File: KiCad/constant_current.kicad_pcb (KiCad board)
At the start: 2 copper layers, 15.2 x 16.5 mm, 18 parts, among them Q1 BC817-40

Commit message: Minor Layout changes
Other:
- board text added: "rev06092017"
- board text removed: "rev05092017"
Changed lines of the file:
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@@
   (general
     (links 24)
-    (no_connects 0)
+    (no_connects 1)
     (area 109.144999 56.439999 124.535001 73.100001)
     (thickness 1.6)
@@
     (effects (font (size 0.7 0.7) (thickness 0.1)) (justify mirror))
   )
-  (gr_text "rev05092017\n" (at 113.538 71.755) (layer B.SilkS)
+  (gr_text "rev06092017\n" (at 113.538 71.755) (layer B.SilkS)
     (effects (font (size 0.7 0.7) (thickness 0.1)) (justify mirror))
   )

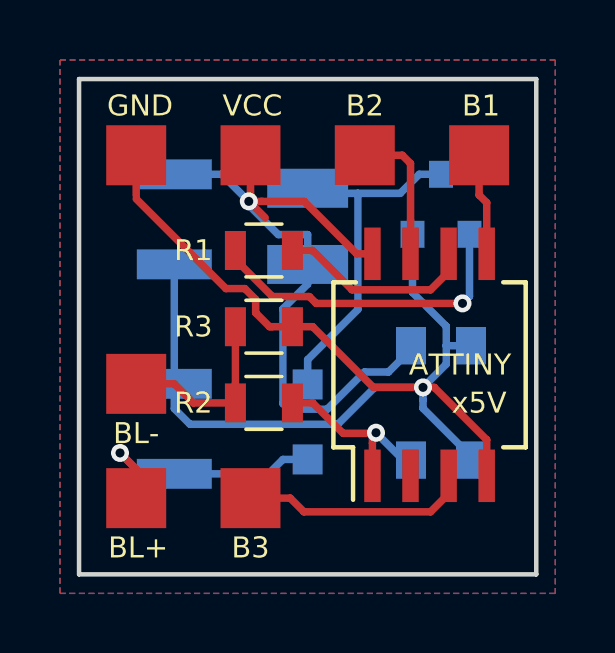
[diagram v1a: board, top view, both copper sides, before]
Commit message: changed diode footprint
Changed the diode footprint to Minimelf
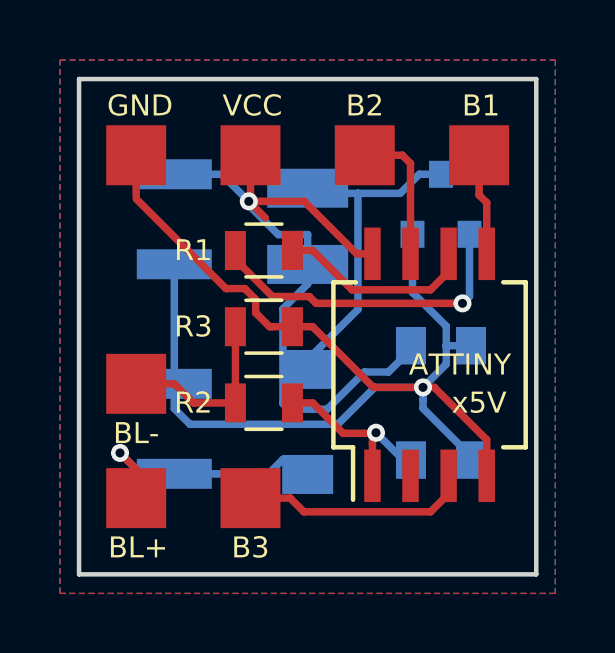
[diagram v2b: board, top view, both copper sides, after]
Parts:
- D1: footprint Diodes_SMD:D_SOD-323_HandSoldering -> Diodes_SMD:D_MiniMELF
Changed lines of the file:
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@@
     (pad_to_mask_clearance 0)
     (aux_axis_origin 0 0)
-    (visible_elements 7FFFFF5F)
+    (visible_elements 7FFFFD5F)
     (pcbplotparams
       (layerselection 0x010fc_80000001)
@@
     )
   )
-  (module Diodes_SMD:D_SOD-323_HandSoldering (layer B.Cu)
-    (at 116.84 67.945 90)
-    (descr SOD-323)
-    (tags SOD-323)
-    (attr smd)
-    (fp_text reference D1 (at 2.54 0 180) (layer B.SilkS)
-      (effects (font (size 0.7 0.7) (thickness 0.1)) (justify mirror))
-    )
-    (fp_text value D (at 0.1 -1.9 90) (layer B.Fab) hide
-      (effects (font (size 1 1) (thickness 0.15)) (justify mirror))
-    )
-    (fp_text user %R (at 0 1.85 90) (layer B.Fab)
-      (effects (font (size 1 1) (thickness 0.15)) (justify mirror))
-    )
-    (fp_line (start -1.9 0.85) (end -1.9 -0.85) (layer B.SilkS) (width 0.12))
-    (fp_line (start 0.2 0) (end 0.45 0) (layer B.Fab) (width 0.1))
-    (fp_line (start 0.2 -0.35) (end -0.3 0) (layer B.Fab) (width 0.1))
-    (fp_line (start 0.2 0.35) (end 0.2 -0.35) (layer B.Fab) (width 0.1))
-    (fp_line (start -0.3 0) (end 0.2 0.35) (layer B.Fab) (width 0.1))
-    (fp_line (start -0.3 0) (end -0.5 0) (layer B.Fab) (width 0.1))
-    (fp_line (start -0.3 0.35) (end -0.3 -0.35) (layer B.Fab) (width 0.1))
-    (fp_line (start -0.9 -0.7) (end -0.9 0.7) (layer B.Fab) (width 0.1))
-    (fp_line (start 0.9 -0.7) (end -0.9 -0.7) (layer B.Fab) (width 0.1))
-    (fp_line (start 0.9 0.7) (end 0.9 -0.7) (layer B.Fab) (width 0.1))
-    (fp_line (start -0.9 0.7) (end 0.9 0.7) (layer B.Fab) (width 0.1))
-    (fp_line (start -2 0.95) (end 2 0.95) (layer B.CrtYd) (width 0.05))
-    (fp_line (start 2 0.95) (end 2 -0.95) (layer B.CrtYd) (width 0.05))
-    (fp_line (start -2 -0.95) (end 2 -0.95) (layer B.CrtYd) (width 0.05))
-    (fp_line (start -2 0.95) (end -2 -0.95) (layer B.CrtYd) (width 0.05))
-    (fp_line (start -1.9 -0.85) (end 1.25 -0.85) (layer B.SilkS) (width 0.12))
-    (fp_line (start -1.9 0.85) (end 1.25 0.85) (layer B.SilkS) (width 0.12))
-    (pad 1 smd rect (at -1.25 0 90) (size 1 1) (layers B.Cu B.Paste B.Mask)
-      (net 11 "Net-(C2-Pad1)"))
-    (pad 2 smd rect (at 1.25 0 90) (size 1 1) (layers B.Cu B.Paste B.Mask)
-      (net 3 "Net-(D1-Pad2)"))
-    (model ${KISYS3DMOD}/Diodes_SMD.3dshapes/D_SOD-323.wrl
-      (at (xyz 0 0 0))
-      (scale (xyz 1 1 1))
-      (rotate (xyz 0 0 0))
-    )
-  )
   (module Capacitors_SMD:C_1210 (layer B.Cu)
     (at 112.395 61.19 90)
@@
     )
   )
-  (gr_line (start 115.951 70.231) (end 117.729 70.231) (layer B.SilkS) (width 0.2))
+  (module Diodes_SMD:D_MiniMELF (layer B.Cu)
+    (at 116.84 67.945 90)
+    (descr "Diode Mini-MELF")
+    (tags "Diode Mini-MELF")
+    (attr smd)
+    (fp_text reference D1 (at 3.1115 0 180) (layer B.SilkS)
+      (effects (font (size 0.7 0.7) (thickness 0.1)) (justify mirror))
+    )
+    (fp_text value D (at 0 -1.75 90) (layer B.Fab)
+      (effects (font (size 1 1) (thickness 0.15)) (justify mirror))
+    )
+    (fp_text user %R (at 0 2 90) (layer B.Fab)
+      (effects (font (size 1 1) (thickness 0.15)) (justify mirror))
+    )
+    (fp_line (start 1.75 1) (end -2.55 1) (layer B.SilkS) (width 0.12))
+    (fp_line (start -2.55 1) (end -2.55 -1) (layer B.SilkS) (width 0.12))
+    (fp_line (start -2.55 -1) (end 1.75 -1) (layer B.SilkS) (width 0.12))
+    (fp_line (start 1.65 0.8) (end 1.65 -0.8) (layer B.Fab) (width 0.1))
+    (fp_line (start 1.65 -0.8) (end -1.65 -0.8) (layer B.Fab) (width 0.1))
+    (fp_line (start -1.65 -0.8) (end -1.65 0.8) (layer B.Fab) (width 0.1))
+    (fp_line (start -1.65 0.8) (end 1.65 0.8) (layer B.Fab) (width 0.1))
+    (fp_line (start 0.25 0) (end 0.75 0) (layer B.Fab) (width 0.1))
+    (fp_line (start 0.25 -0.4) (end -0.35 0) (layer B.Fab) (width 0.1))
+    (fp_line (start 0.25 0.4) (end 0.25 -0.4) (layer B.Fab) (width 0.1))
+    (fp_line (start -0.35 0) (end 0.25 0.4) (layer B.Fab) (width 0.1))
+    (fp_line (start -0.35 0) (end -0.35 -0.55) (layer B.Fab) (width 0.1))
+    (fp_line (start -0.35 0) (end -0.35 0.55) (layer B.Fab) (width 0.1))
+    (fp_line (start -0.75 0) (end -0.35 0) (layer B.Fab) (width 0.1))
+    (fp_line (start -2.65 1.1) (end 2.65 1.1) (layer B.CrtYd) (width 0.05))
+    (fp_line (start 2.65 1.1) (end 2.65 -1.1) (layer B.CrtYd) (width 0.05))
+    (fp_line (start 2.65 -1.1) (end -2.65 -1.1) (layer B.CrtYd) (width 0.05))
+    (fp_line (start -2.65 -1.1) (end -2.65 1.1) (layer B.CrtYd) (width 0.05))
+    (pad 1 smd rect (at -1.75 0 90) (size 1.3 1.7) (layers B.Cu B.Paste B.Mask)
+      (net 11 "Net-(C2-Pad1)"))
+    (pad 2 smd rect (at 1.75 0 90) (size 1.3 1.7) (layers B.Cu B.Paste B.Mask)
+      (net 3 "Net-(D1-Pad2)"))
+    (model ${KISYS3DMOD}/Diodes_SMD.3dshapes/D_MiniMELF.wrl
+      (at (xyz 0 0 0))
+      (scale (xyz 1 1 1))
+      (rotate (xyz 0 0 0))
+    )
+  )
+  (gr_line (start 115.7605 70.8025) (end 117.9195 70.8025) (layer B.SilkS) (width 0.2))
   (gr_text rcb_4s (at 121.92 71.755) (layer B.SilkS)
     (effects (font (size 0.7 0.7) (thickness 0.1)) (justify mirror))

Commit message: Code and Layout fixes
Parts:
- D1: footprint Diodes_SMD:D_MiniMELF -> Diodes_SMD:D_SOD-323_HandSoldering
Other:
- board text added: "rev14092017"
- board text removed: "rev06092017"
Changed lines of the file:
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@@
     (links 24)
     (no_connects 1)
-    (area 109.144999 56.439999 124.535001 73.100001)
+    (area 108.585 54.57988 126.109 73.660001)
     (thickness 1.6)
     (drawings 8)
@@
     (pad_to_mask_clearance 0)
     (aux_axis_origin 0 0)
-    (visible_elements 7FFFFD5F)
+    (visible_elements 7FFFFD7F)
     (pcbplotparams
       (layerselection 0x010fc_80000001)
@@
       (drillshape 0)
       (scaleselection 1)
-      (outputdirectory gerber/panel/))
+      (outputdirectory ../gerber/))
   )
   (net 0 "")
@@
     (tags "capacitor 1210")
     (attr smd)
-    (fp_text reference C1 (at 2.667 0 180) (layer B.SilkS)
+    (fp_text reference C1 (at 2.77 0 180) (layer B.SilkS)
       (effects (font (size 0.7 0.7) (thickness 0.1)) (justify mirror))
     )
@@
     )
   )
-  (module Diodes_SMD:D_MiniMELF (layer B.Cu)
+  (module Diodes_SMD:D_SOD-323_HandSoldering (layer B.Cu)
     (at 116.84 67.945 90)
-    (descr "Diode Mini-MELF")
-    (tags "Diode Mini-MELF")
-    (attr smd)
-    (fp_text reference D1 (at 3.1115 0 180) (layer B.SilkS)
+    (descr SOD-323)
+    (tags SOD-323)
+    (attr smd)
+    (fp_text reference D1 (at 2.54 0 180) (layer B.SilkS)
       (effects (font (size 0.7 0.7) (thickness 0.1)) (justify mirror))
     )
-    (fp_text value D (at 0 -1.75 90) (layer B.Fab)
-      (effects (font (size 1 1) (thickness 0.15)) (justify mirror))
-    )
-    (fp_text user %R (at 0 2 90) (layer B.Fab)
-      (effects (font (size 1 1) (thickness 0.15)) (justify mirror))
-    )
-    (fp_line (start 1.75 1) (end -2.55 1) (layer B.SilkS) (width 0.12))
-    (fp_line (start -2.55 1) (end -2.55 -1) (layer B.SilkS) (width 0.12))
-    (fp_line (start -2.55 -1) (end 1.75 -1) (layer B.SilkS) (width 0.12))
-    (fp_line (start 1.65 0.8) (end 1.65 -0.8) (layer B.Fab) (width 0.1))
-    (fp_line (start 1.65 -0.8) (end -1.65 -0.8) (layer B.Fab) (width 0.1))
-    (fp_line (start -1.65 -0.8) (end -1.65 0.8) (layer B.Fab) (width 0.1))
-    (fp_line (start -1.65 0.8) (end 1.65 0.8) (layer B.Fab) (width 0.1))
-    (fp_line (start 0.25 0) (end 0.75 0) (layer B.Fab) (width 0.1))
-    (fp_line (start 0.25 -0.4) (end -0.35 0) (layer B.Fab) (width 0.1))
-    (fp_line (start 0.25 0.4) (end 0.25 -0.4) (layer B.Fab) (width 0.1))
-    (fp_line (start -0.35 0) (end 0.25 0.4) (layer B.Fab) (width 0.1))
-    (fp_line (start -0.35 0) (end -0.35 -0.55) (layer B.Fab) (width 0.1))
-    (fp_line (start -0.35 0) (end -0.35 0.55) (layer B.Fab) (width 0.1))
-    (fp_line (start -0.75 0) (end -0.35 0) (layer B.Fab) (width 0.1))
-    (fp_line (start -2.65 1.1) (end 2.65 1.1) (layer B.CrtYd) (width 0.05))
-    (fp_line (start 2.65 1.1) (end 2.65 -1.1) (layer B.CrtYd) (width 0.05))
-    (fp_line (start 2.65 -1.1) (end -2.65 -1.1) (layer B.CrtYd) (width 0.05))
-    (fp_line (start -2.65 -1.1) (end -2.65 1.1) (layer B.CrtYd) (width 0.05))
-    (pad 1 smd rect (at -1.75 0 90) (size 1.3 1.7) (layers B.Cu B.Paste B.Mask)
+    (fp_text value D (at 0.1 -1.9 90) (layer B.Fab)
+      (effects (font (size 1 1) (thickness 0.15)) (justify mirror))
+    )
+    (fp_text user %R (at 0 1.85 90) (layer B.Fab)
+      (effects (font (size 1 1) (thickness 0.15)) (justify mirror))
+    )
+    (fp_line (start -1.9 0.85) (end -1.9 -0.85) (layer B.SilkS) (width 0.12))
+    (fp_line (start 0.2 0) (end 0.45 0) (layer B.Fab) (width 0.1))
+    (fp_line (start 0.2 -0.35) (end -0.3 0) (layer B.Fab) (width 0.1))
+    (fp_line (start 0.2 0.35) (end 0.2 -0.35) (layer B.Fab) (width 0.1))
+    (fp_line (start -0.3 0) (end 0.2 0.35) (layer B.Fab) (width 0.1))
+    (fp_line (start -0.3 0) (end -0.5 0) (layer B.Fab) (width 0.1))
+    (fp_line (start -0.3 0.35) (end -0.3 -0.35) (layer B.Fab) (width 0.1))
+    (fp_line (start -0.9 -0.7) (end -0.9 0.7) (layer B.Fab) (width 0.1))
+    (fp_line (start 0.9 -0.7) (end -0.9 -0.7) (layer B.Fab) (width 0.1))
+    (fp_line (start 0.9 0.7) (end 0.9 -0.7) (layer B.Fab) (width 0.1))
+    (fp_line (start -0.9 0.7) (end 0.9 0.7) (layer B.Fab) (width 0.1))
+    (fp_line (start -2 0.95) (end 2 0.95) (layer B.CrtYd) (width 0.05))
+    (fp_line (start 2 0.95) (end 2 -0.95) (layer B.CrtYd) (width 0.05))
+    (fp_line (start -2 -0.95) (end 2 -0.95) (layer B.CrtYd) (width 0.05))
+    (fp_line (start -2 0.95) (end -2 -0.95) (layer B.CrtYd) (width 0.05))
+    (fp_line (start -1.9 -0.85) (end 1.25 -0.85) (layer B.SilkS) (width 0.12))
+    (fp_line (start -1.9 0.85) (end 1.25 0.85) (layer B.SilkS) (width 0.12))
+    (pad 1 smd rect (at -1.25 0 90) (size 1 1) (layers B.Cu B.Paste B.Mask)
       (net 11 "Net-(C2-Pad1)"))
-    (pad 2 smd rect (at 1.75 0 90) (size 1.3 1.7) (layers B.Cu B.Paste B.Mask)
+    (pad 2 smd rect (at 1.25 0 90) (size 1 1) (layers B.Cu B.Paste B.Mask)
       (net 3 "Net-(D1-Pad2)"))
-    (model ${KISYS3DMOD}/Diodes_SMD.3dshapes/D_MiniMELF.wrl
-      (at (xyz 0 0 0))
-      (scale (xyz 1 1 1))
-      (rotate (xyz 0 0 0))
-    )
-  )
-  (gr_line (start 115.7605 70.8025) (end 117.9195 70.8025) (layer B.SilkS) (width 0.2))
+    (model ${KISYS3DMOD}/Diodes_SMD.3dshapes/D_SOD-323.wrl
+      (at (xyz 0 0 0))
+      (scale (xyz 1 1 1))
+      (rotate (xyz 0 0 0))
+    )
+  )
+  (gr_line (start 115.7605 70.2945) (end 117.9195 70.2945) (layer B.SilkS) (width 0.2))
   (gr_text rcb_4s (at 121.92 71.755) (layer B.SilkS)
     (effects (font (size 0.7 0.7) (thickness 0.1)) (justify mirror))
   )
-  (gr_text "rev06092017\n" (at 113.538 71.755) (layer B.SilkS)
+  (gr_text "rev14092017\n" (at 113.538 71.755) (layer B.SilkS)
     (effects (font (size 0.7 0.7) (thickness 0.1)) (justify mirror))
   )
